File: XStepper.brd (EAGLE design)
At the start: 102 x 82 mm, 95 parts, among them IC1 L7805, IC2 L7812, Q2 16 MHZ, U1 FT232RL-BASICSSOP

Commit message: - some changes from matt and produce in fab 0.95
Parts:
- removed C14, C15: 18pF, resistor:C025-025X050
- removed C16: 0.1uF, resistor:C025-025X050
- removed C17, C19: 0.1uF, SparkFun-Capacitors:1206
- removed C9: 100uF, resistor:E2,5-6
- removed R11: 220, SparkFun-Resistors:AXIAL-0.3
- removed R13, R14: 10K, SparkFun-Resistors:1206
- removed R3, R6, R7: 330, SparkFun-Resistors:AXIAL-0.3
- removed R5: 110, SparkFun-Resistors:AXIAL-0.3
- removed R8, R9: 1K, SparkFun-Resistors:1206
- added C22, C30, C31: 0.1uF, resistor:C025-025X050
- added C32: 10uF, SparkFun-Capacitors:EIA3216
- added C33, C34: 0.1uF, SparkFun-Capacitors:1206
- added JP9: (no value), SparkFun-Connectors:1X02
- added R21, R32, R33: 330, SparkFun-Resistors:AXIAL-0.3
- added R30, R31: 470, SparkFun-Resistors:AXIAL-0.3
- added R34, R35: 10K, SparkFun-Resistors:1206
- added R36, R37: 1K, SparkFun-Resistors:1206
- added SJ1: NO, SparkFun-Passives:SJ_2S-NO
- A-AXIS, X-AXIS, Y-AXIS, Z-AXIS: value 2x03 -> (none)
- AD, XD, YD, ZD: value green -> Gr
- C1: value 0.1uF -> 18pF
- C10: value 47uF -> 200uF; device resistor:E2,5-6 -> resistor:E3,5-8
- C11: value 0.1uF -> 100uF; device resistor:C025-025X050 -> resistor:E2,5-6
- C12: value 0.1uF -> 47uF; device resistor:C025-025X050 -> resistor:E2,5-6
- C2: value 100uF -> 18pF; device resistor:E3,5-8 -> resistor:C025-025X050
- C20: value 10uF -> 0.1uF; device SparkFun-Capacitors:EIA3216 -> resistor:C025-025X050
- C21: value 200uF -> 100uF
- R10, R25: value 220 -> 330
- R22: value 470 -> 110
- R23: value 470 -> 330
- VCC: value orange -> Or
- X, Y, Z: value red -> Rd
- moved C13 85.2 mm to (8.89, 16.5)
- moved C2 64.9 mm to (54.6, 19.1), turned to 270 degrees
- moved C20 63.3 mm to (26.2, 64.2), turned to 0 degrees
- moved R22 55.8 mm to (44.7, 45.9), turned to 0 degrees
- moved C1 52.1 mm to (52.1, 19.1), turned to 270 degrees
- moved C3 40.8 mm to (45.0, 23.5), turned to 90 degrees
- moved R10 35.1 mm to (20.3, 11.4), turned to 0 degrees
- moved C21 33.2 mm to (12.0, 68.0), turned to 270 degrees
- moved R23 26.7 mm to (62.4, 4.83), turned to 90 degrees
- moved C12 26.2 mm to (20.3, 17.8)
- moved JP6 23.9 mm to (87.1, 12.4)
- moved C10 16.6 mm to (20.3, 34.3), turned to 270 degrees
- moved SJ4 16.3 mm to (90.2, 12.3)
- moved C11 14.5 mm to (20.3, 25.4)
- moved TX 8.13 mm to (89.6, 42.9)
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- renumbered C4 to C23, C5 to C24, C6 to C25, C7 to C26, C8 to C27, R12 to R25, R15 to R24, R16 to R26, R4 to R20
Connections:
- new net N$10: SJ1.1, TTL.2
- new net USB_GND: C32.C, C33.2, C34.2, JP7.GND, JP8.GND, JP9.1, SJ1.2, SJ4.2, TTL.1, U1.18, U1.21, U1.25, U1.26, U1.7
- net +12V: now also C11.+; no longer C9.+
- net 5V: now also C12.+, C13.2, C20.1, C22.1, C3.2, C31.2, R10.P$2, R32.P$2, R36.2, R37.2; no longer C1.1, C10.+, C11.2, C12.2, C16.2, C3.1, R3.P$2, R6.P$2, R8.2, R9.2
- net DTR: now also C30.1, R35.2; no longer C13.1, R13.2
- net FTDI_TX: now also R34.2; no longer R14.2
- net GND: now also C11.-, C12.-, C13.1, C2.2, C20.2, C22.2, C3.1, C31.1, JP9.2, R22.P$2; no longer C11.1, C12.1, C14.2, C15.2, C16.1, C17.2, C19.2, C2.-, C20.C, C3.2, C9.-, JP7.GND, JP8.GND, R5.P$2, SJ4.2, TTL.1, U1.18, U1.21, U1.25, U1.26, U1.7
- net N$1: now also C34.1; no longer C17.1
- net N$17: now also R37.1; no longer R9.1
- net N$18: now also R36.1; no longer R8.1
- net N$25: now also R22.P$1; no longer R5.P$1
- net N$33: now also C1.1; no longer C15.1
- net N$34: now also C2.1; no longer C14.1
- net N$35: now also R21.P$2; no longer R10.P$2
- net N$36: now also R23.P$2; no longer R11.P$2
- net N$4: now also R35.1; no longer R13.1
- net N$43: now also R10.P$1; no longer R3.P$1
- net N$46: now also R31.P$2; no longer R23.P$2
- net N$47: now also R30.P$2; no longer R22.P$2
- net N$9: now also R34.1; no longer R14.1
- net OPTO_RX: now also R33.P$1; no longer R7.P$1
- net OPTO_TX: now also R30.P$1; no longer R22.P$1
- net RESET: now also C30.2; no longer C13.2
- net RXD_USB: now also R31.P$1; no longer R23.P$1
- net TTL/USB_5V: now also C32.A, C33.1, R33.P$2; no longer C19.1, C20.A, R7.P$2
- net TXD_USB: now also R32.P$1; no longer R6.P$1
- net VIN: now also C10.+; no longer C21.+
- net VMOT: now also C21.+; no longer C2.+
- net X-STOP: now also R21.P$1; no longer R10.P$1
- net Y-STOP: now also R23.P$1; no longer R11.P$1
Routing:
- net RXD_USB: track 56.1 -> 9.85 mm
- net 5V: track 437.5 -> 403.9 mm
- net USB_GND: track 0.00 -> 28.1 mm, vias 0 -> 6
- net SPINDLE-DIR: track 112.7 -> 132.8 mm
- net OPTO_TX: track 31.5 -> 12.0 mm
- net TTL/USB_5V: track 108.7 -> 90.0 mm
- net TTL_RX: track 29.3 -> 11.9 mm
- net TTL_TX: track 28.9 -> 11.9 mm
- net FTDI_RX: track 22.1 -> 6.76 mm, vias 1 -> 0
- net FTDI_TX: track 19.9 -> 5.04 mm
- net SPINDLE-ENABLE: track 130.3 -> 116.5 mm, vias 1 -> 0
- net N$11: track 14.9 -> 26.5 mm
- net ENABLE: track 150.2 -> 138.8 mm
- net GND: track 11.1 -> 0.19 mm, vias 13 -> 1
- net RESET: track 104.3 -> 93.6 mm
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- added copper zone on layer 1, net USB_GND
- added copper zone on layer 16, net USB_GND
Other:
- board text added: "DTR"
- board text added: "RX"
- board text added: "TX"
- board text added: "XStepper 0.95P"
- board text removed: "XStepper 0.95k"

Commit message: - gerber files for ITEAD 0.96
- new pic for docs
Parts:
- removed EN: EN, SparkFun-Passives:SJ_2W
- removed S1: (no value), SparkFun-Electromechanical:TACTILE_SWITCH_SMD
- added S2: (no value), SparkFun-Electromechanical:TACTILE_SWITCH_SMD
- added STEP: EN, SparkFun-Passives:SJ_2W
- JP5, JP6: device SparkFun-Connectors:2X3_POGO -> pinhead:2X03
- JP9: value (none) -> M02PTH
- moved JP5 34.9 mm to (71.1, 34.3), turned to 90 degrees
- moved R33 13.0 mm to (65.5, 13.7), turned to 180 degrees
- moved C31 12.4 mm to (73.0, 26.6), turned to 0 degrees
- moved R31 9.95 mm to (62.0, 20.1), turned to 270 degrees
- moved TX 8.13 mm to (83.2, 37.9)
- moved R32 7.93 mm to (76.5, 29.2), turned to 270 degrees
- moved R2 6.55 mm to (65.7, 33.0)
- moved C1 4.41 mm to (48.3, 21.3), turned to 180 degrees
- moved R20 3.28 mm to (20.5, 46.0)
- moved R22 3.17 mm to (41.5, 46.0)
- moved R24 3.14 mm to (62.5, 46.0)
- moved R26 3.06 mm to (83.5, 46.0)
- moved 328P 2.84 mm to (45.7, 33.0)
- moved RX 2.84 mm to (88.3, 37.9)
- moved JP6 2.83 mm to (84.6, 11.1)
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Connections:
- net 5V: no longer R36.2, R37.2
- net A-STEP: now also STEP.2; no longer EN.2
- net BT_RXD: now also JP5.6; no longer JP5.P$6
- net BT_TXD: now also JP5.5; no longer JP5.P$5
- net FTDI_RX: now also JP6.6; no longer JP6.P$6
- net FTDI_TX: now also JP6.5; no longer JP6.P$5
- net GND: now also S2.1, S2.2; no longer S1.1, S1.2
- net OPTO_RX: now also JP6.4; no longer JP6.P$4
- net OPTO_TX: now also JP6.3; no longer JP6.P$3
- net RESET: now also S2.3, S2.4; no longer S1.3, S1.4
- net RX: now also JP5.3; no longer JP5.P$3
- net RXD_USB: now also JP5.2; no longer JP5.P$2
- net SPINDLE-ENABLE: now also STEP.1; no longer EN.1
- net TTL/USB_5V: now also R36.2, R37.2
- net TTL_RX: now also JP6.2; no longer JP6.P$2
- net TTL_TX: now also JP6.1; no longer JP6.P$1
- net TX: now also JP5.4; no longer JP5.P$4
- net TXD_USB: now also JP5.1; no longer JP5.P$1
- net Y-STEP: now also STEP.3; no longer EN.3
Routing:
- net GND: track 0.19 -> 49.4 mm, vias 1 -> 5
- net BT_TXD: track 72.3 -> 27.3 mm, vias 1 -> 0
- net TX: track 13.3 -> 56.3 mm
- net RX: track 18.4 -> 60.1 mm
- net TXD_USB: track 56.4 -> 17.0 mm
- net 5V: track 403.9 -> 438.6 mm, vias 0 -> 4
- net BT_RXD: track 64.5 -> 30.9 mm
- net TTL/USB_5V: track 90.0 -> 121.9 mm, vias 0 -> 2
- net USB_GND: track 28.1 -> 9.32 mm, vias 6 -> 3
- net SPINDLE-ENABLE: track 116.5 -> 130.5 mm, vias 0 -> 1
- net G-RESET: track 47.5 -> 37.5 mm, vias 0 -> 1
- net RESERVED: track 35.4 -> 44.8 mm
- net N$46: track 13.9 -> 4.90 mm
- net ENABLE: track 138.8 -> 147.8 mm, vias 0 -> 5
- net COOLANT-FLOOD: track 42.5 -> 51.4 mm
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- removed copper zone on layer 1, net GND
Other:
- board size 102 x 82 mm -> 99.7 x 82 mm
- board text added: "+"
- board text added: "-"
- board text added: "XStepper 0.96"
- board text removed: "XStepper 0.95P"

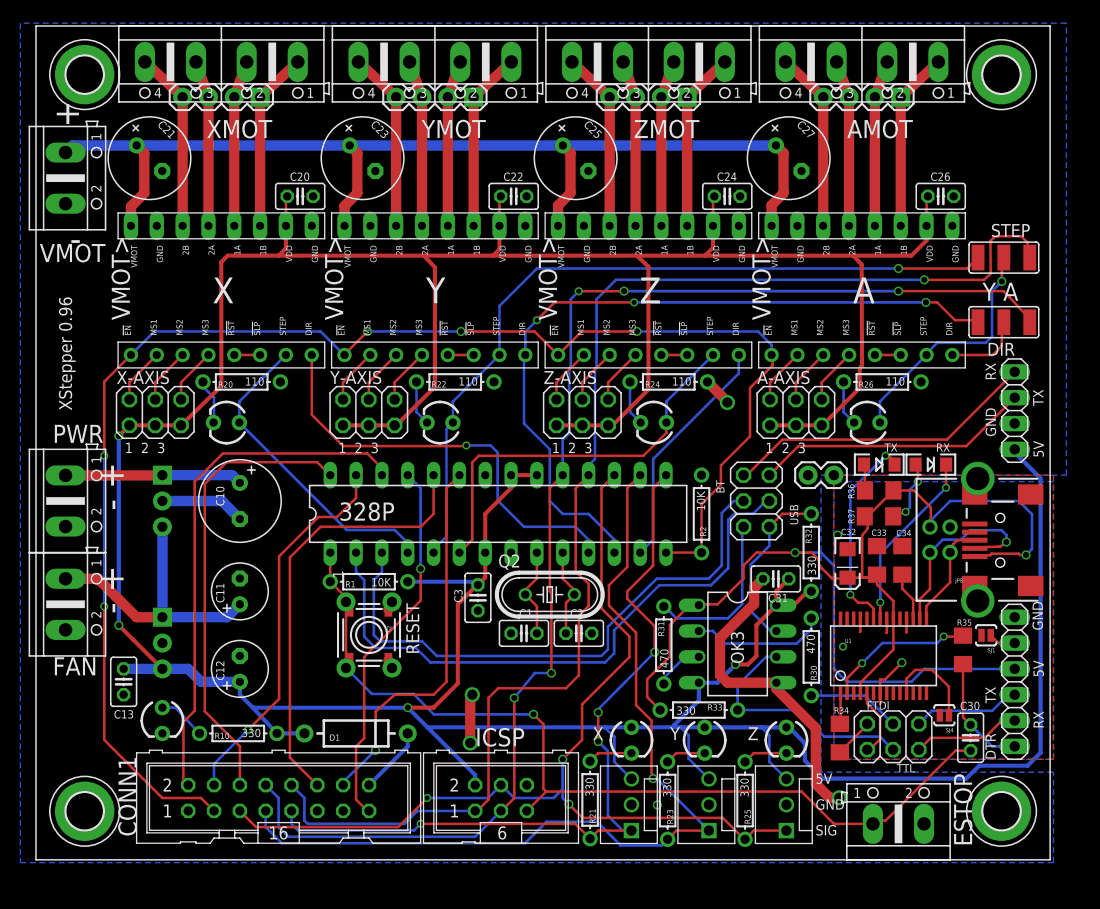
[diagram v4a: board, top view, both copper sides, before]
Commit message: - version 0.97 to fab
*On-board USB in now in the bottom of the board
*USB isolation header moved.
*Bluetooth header moved
*Bluetooth dip/jumpers removed - bluetooth is always-on
*FTDI header moved
*FTDI now can be tied to 5V and GND for isolation or to forego isolation
and directly power the board logic from USB
*Pololu jumpers now separated (I forgot that this was a requirement and
not an option)
*Removed endstop status LED's
*Removed 16-pin header
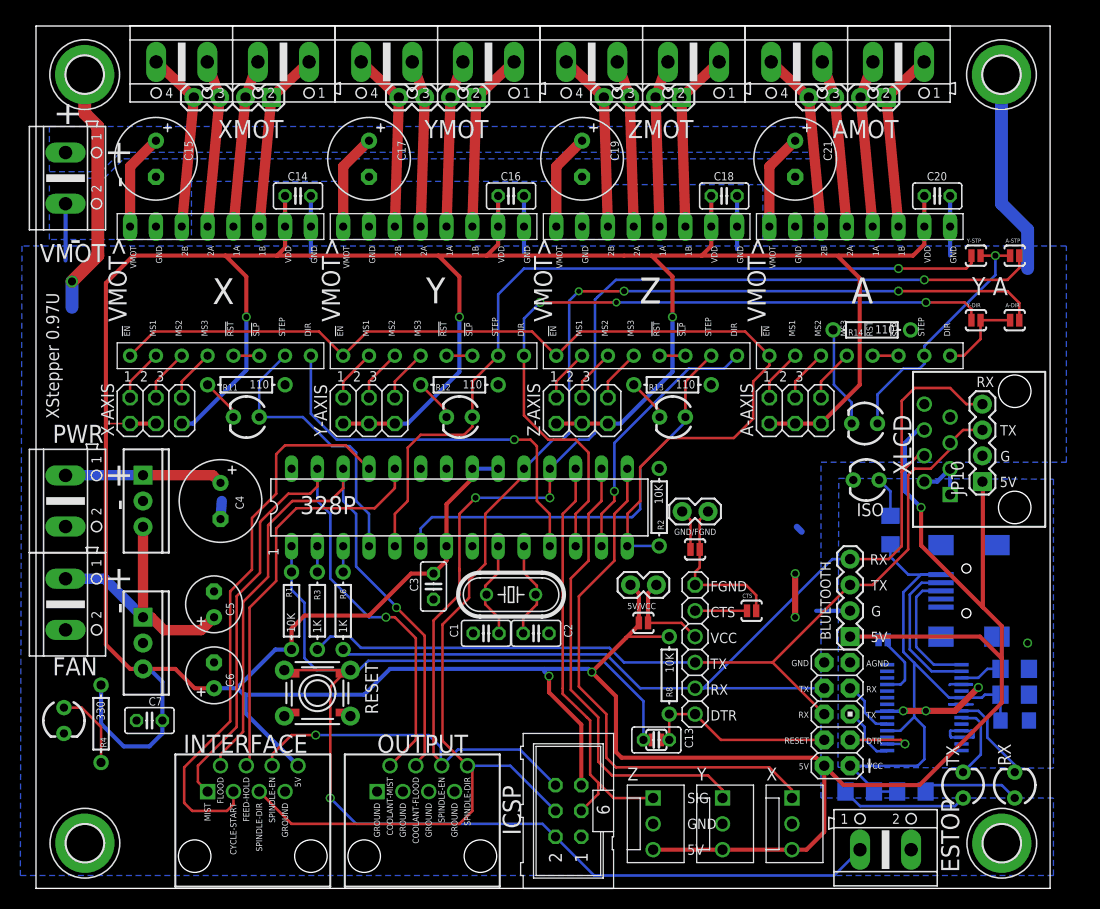
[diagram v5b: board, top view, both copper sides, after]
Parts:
- removed BT-TTL: (no value), pinhead:1X04
- removed C22, C24, C26, C30, C31: 0.1uF, resistor:C025-025X050
- removed C23, C25, C27: 100uF, resistor:E3,5-8
- removed C32: 10uF, SparkFun-Capacitors:EIA3216
- removed C33, C34: 0.1uF, SparkFun-Capacitors:1206
- removed CONN1: (no value), con-ml:ML16
- removed D1: (no value), SparkFun-DiscreteSemi:DIODE-1N4001
- removed DIR: DIR, SparkFun-Passives:SJ_2W
- removed ICSP: (no value), con-ml:ML6
- removed JP8: USB-B, SparkFun-Connectors:USB-B-PTH
- removed OK3: HCPL2630, optocoupler:DIL08
- removed R20, R22, R24, R26: 110, SparkFun-Resistors:AXIAL-0.3
- removed R21, R23, R25, R32, R33: 330, SparkFun-Resistors:AXIAL-0.3
- removed R30, R31: 470, SparkFun-Resistors:AXIAL-0.3
- removed R34, R35: 10K, SparkFun-Resistors:1206
- removed R36, R37: 1K, SparkFun-Resistors:1206
- removed SJ1, SJ4: NO, SparkFun-Passives:SJ_2S-NO
- removed STEP: EN, SparkFun-Passives:SJ_2W
- removed TTL: GND, pinhead:1X06
- removed X, Y, Z: Rd, SparkFun-LED:LED3MM
- added 5V, A-DIR, A-STP, CTS, CTS-FTDI, DTR, GND, Y-DIR, Y-STP: NO, SparkFun-Passives:SJ_2S-NO
- added C14, C16, C18, C7: 0.1uF, resistor:C025-025X050
- added C15, C17, C19: 100uF, resistor:E3,5-8
- added C4: 200uF, resistor:E3,5-8
- added C5: 100uF, resistor:E2,5-6
- added C6: 47uF, resistor:E2,5-6
- added ISO: (no value), SparkFun-LED:LED3MM
- added JP10, JP11: (no value), SparkFun-Connectors:1X04
- added JP12: (no value), pinhead:1X06
- added R11, R12, R13, R14: 110, SparkFun-Resistors:AXIAL-0.3
- added R3, R6: 1K, SparkFun-Resistors:AXIAL-0.3
- added R4: 330, SparkFun-Resistors:AXIAL-0.3
- added R5, R9: 1K, SparkFun-Resistors:1206
- added R8: 10K, SparkFun-Resistors:AXIAL-0.3
- added SV1: (no value), con-ml:ML6
- added U$14, U$2, U$8: TYCO 5555164-1, SparkFun-Connectors:RJ45-8
- C10: value 200uF -> 10uF; device resistor:E3,5-8 -> SparkFun-Capacitors:EIA3216
- C11: value 100uF -> 0.1uF; device resistor:E2,5-6 -> SparkFun-Capacitors:1206
- C12: value 47uF -> 0.1uF; device resistor:E2,5-6 -> SparkFun-Capacitors:1206
- JP5: value (none) -> M05X2PTH; device pinhead:2X03 -> SparkFun-Connectors:AVR_ICSP
- JP6: value (none) -> M02PTH; device pinhead:2X03 -> SparkFun-Connectors:1X02
- R10: value 330 -> 1K; device SparkFun-Resistors:AXIAL-0.3 -> SparkFun-Resistors:1206
- RX: value Grn -> (none); device SparkFun-LED:LED-1206 -> SparkFun-LED:LED3MM
- TX: value Red -> (none); device SparkFun-LED:LED-1206 -> SparkFun-LED:LED3MM
- moved C10 79.2 mm to (96.5, 12.7), flipped to the bottom, turned to 0 degrees
- moved C11 76.9 mm to (96.5, 15.2), flipped to the bottom, turned to 180 degrees
- moved C12 76.2 mm to (96.5, 17.8), flipped to the bottom, turned to 180 degrees
- moved C21 63.5 mm to (74.9, 67.9), turned to 270 degrees
- moved C20 62.7 mm to (88.9, 64.3)
- moved R10 61.4 mm to (81.3, 5.71), flipped to the bottom, turned to 180 degrees
- moved C13 52.7 mm to (61.3, 10.8), turned to 180 degrees
- moved RX 32.6 mm to (96.5, 6.35), turned to 90 degrees
- moved TX 32.6 mm to (91.4, 6.35), turned to 90 degrees
- moved JP6 27.7 mm to (61.3, 26.0)
- moved JP5 22.4 mm to (79.1, 13.3), turned to 180 degrees
- moved XLIM 16.1 mm to (74.6, 5.08), turned to 270 degrees
- moved JP9 15.3 mm to (63.8, 33.3), turned to 0 degrees
- moved ZLIM 13.5 mm to (61.0, 5.08), turned to 270 degrees
- moved VCC 9.68 mm to (3.02, 12.7)
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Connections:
- removed net BT_RXD: BT-TTL.4, JP5.6
- removed net BT_TXD: BT-TTL.3, JP5.5
- removed net N$35: R21.P$2, X.K
- removed net N$36: R23.P$2, Y.K
- removed net N$37: R25.P$2, Z.K
- removed net N$45: CONN1.16, D1.C
- removed net N$46: OK3.3, R31.P$2
- removed net N$47: OK3.2, R30.P$2
- removed net OPTO_RX: JP6.4, OK3.6, R33.P$1
- removed net OPTO_TX: JP6.3, R30.P$1
- removed net RXD_USB: JP5.2, R31.P$1
- removed net TTL/USB_5V: C32.A, C33.1, JP7.VBUS, JP8.VBUS, OK3.1, R33.P$2, R36.2, R37.2, TTL.3, U1.20, U1.4
- removed net TTL_RX: JP6.2, TTL.5
- removed net TTL_TX: JP6.1, TTL.4
- removed net TXD_USB: JP5.1, OK3.7, R32.P$1
- removed net USB_GND: C32.C, C33.2, C34.2, JP7.GND, JP8.GND, JP9.1, SJ1.2, SJ4.2, TTL.1, U1.18, U1.21, U1.25, U1.26, U1.7
- removed net VMOT: C21.+, C23.+, C25.+, C27.+, STEPPERDRIVER.VMOT, STEPPERDRIVER1.VMOT, STEPPERDRIVER2.VMOT, STEPPERDRIVER3.VMOT, VMOT.1
- new net AGND: C10.C, C11.2, C12.2, CTS-FTDI.2, ISO.K, JP5.9, JP7.GND, U1.18, U1.21, U1.25, U1.26, U1.7
- new net FTDI_DTR: JP5.3, U1.2
- new net N$40: 328P.3, R6.P$1
- new net N$41: 5V.1, JP12.3, JP6.1
- new net N$44: CTS.2, GND.1, JP12.1, JP9.2
- new net V+: C15.+, C17.+, C19.+, C21.+, STEPPERDRIVER.VMOT, STEPPERDRIVER1.VMOT, STEPPERDRIVER2.VMOT, STEPPERDRIVER3.VMOT, VMOT.1
- new net VCC/2: C10.A, C11.1, JP5.1, JP7.VBUS, R10.2, R5.2, R9.2, U1.20, U1.4
- net +12V: now also C5.+; no longer C11.+
- net 5V: now also 5V.2, C14.1, C16.1, C18.1, C6.+, C7.2, JP10.1, JP11.1, JP5.2, JP6.2, R4.P$2, R8.P$2, SV1.5, U$14.6, U$2.8; no longer BT-TTL.1, C12.+, C13.2, C22.1, C24.1, C26.1, C31.2, D1.A, ICSP.2, OK3.4, OK3.8, R10.P$2, R32.P$2, X.A, Y.A, Z.A
- net A-DIR: now also A-DIR.1, Y-DIR.2; no longer DIR.2
- net A-STEP: now also A-STP.1, Y-STP.2; no longer STEP.2
- net COOLANT-FLOOD: now also U$2.2, U$8.4; no longer CONN1.2
- net COOLANT-MIST: now also U$2.1, U$8.2; no longer CONN1.4
- net CYCLE-START: now also U$2.3; no longer CONN1.15
- net DTR: now also C13.1, DTR.1, JP12.6, JP5.4, R8.P$1; no longer C30.1, R35.2, TTL.6
- net ENABLE: no longer CONN1.3
- net FEED-HOLD: now also U$2.4; no longer CONN1.12
- net FTDI_RX: now also JP5.7; no longer JP6.6
- net FTDI_TX: now also JP5.5, U1.1; no longer JP6.5, R34.2
- net G-RESET: no longer CONN1.14
- net GND: now also C14.2, C15.-, C16.2, C17.-, C18.2, C19.-, C4.-, C5.-, C6.-, C7.1, GND.2, JP10.2, JP11.2, JP5.10, JP9.1, R11.P$2, R12.P$2, R13.P$2, R14.P$2, SV1.1, U$14.1, U$14.2, U$14.3, U$14.7, U$14.8, U$2.7, U$8.1, U$8.3, U$8.5, U$8.7; no longer BT-TTL.2, C10.-, C11.-, C12.-, C13.1, C22.2, C23.-, C24.2, C25.-, C26.2, C27.-, C31.1, CONN1.1, CONN1.11, CONN1.13, ICSP.6, JP9.2, OK3.5, R20.P$2, R22.P$2, R24.P$2, R26.P$2
- net N$1: now also C12.1; no longer C34.1
- net N$10: now also CTS.1, JP12.2; no longer SJ1.1, TTL.2
- net N$11: now also TX.K; no longer TX.C
- net N$12: now also RX.K; no longer RX.C
- net N$17: now also R9.1; no longer R37.1
- net N$18: now also R10.1; no longer R36.1
- net N$19: now also CTS-FTDI.1; no longer SJ4.1
- net N$2: no longer JP8.D+
- net N$20: now also R11.P$1; no longer R20.P$1
- net N$25: now also R12.P$1; no longer R22.P$1
- net N$26: now also R13.P$1; no longer R24.P$1
- net N$28: now also R14.P$1; no longer R26.P$1
- net N$3: no longer JP8.D-
- net N$4: now also ISO.A, R5.1; no longer R35.1, U1.2
- net N$43: now also R4.P$1; no longer R10.P$1
- net N$9: now also 328P.2, R3.P$1; no longer R34.1, U1.1
- net RESERVED: no longer CONN1.6
- net RESET: now also C13.2, DTR.2, SV1.2; no longer C30.2, ICSP.5
- net RX: now also JP10.3, JP11.3, JP12.4, JP5.6, R3.P$2, U$14.5; no longer 328P.2, JP5.3
- net SPINDLE-DIR: now also A-DIR.2, SV1.4, U$2.5, U$8.8; no longer CONN1.8, DIR.3, ICSP.3
- net SPINDLE-ENABLE: now also A-STP.2, SV1.6, U$2.6, U$8.6; no longer CONN1.10, ICSP.1, STEP.1
- net TX: now also JP10.4, JP11.4, JP12.5, JP5.8, R6.P$2, U$14.4; no longer 328P.3, JP5.4
- net VIN: now also C4.+; no longer C10.+
- net X-STOP: no longer CONN1.9, R21.P$1
- net Y-DIR: now also Y-DIR.1; no longer DIR.1
- net Y-STEP: now also Y-STP.1; no longer STEP.3
- net Y-STOP: no longer CONN1.7, R23.P$1
- net Z-STOP: now also SV1.3; no longer CONN1.5, ICSP.4, R25.P$1
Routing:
- net TTL/USB_5V: track 121.9 -> 0.00 mm, vias 2 -> 0
- net VMOT: track 105.1 -> 0.00 mm
- net 5V: track 438.6 -> 525.4 mm, vias 4 -> 6
- net VCC/2: track 0.00 -> 57.8 mm
- net Z-STOP: track 95.2 -> 42.4 mm, vias 3 -> 0
- net ENABLE: track 147.8 -> 100.2 mm, vias 5 -> 0
- net GND: track 49.4 -> 94.7 mm, vias 5 -> 3
- net RESERVED: track 44.8 -> 0.00 mm
- net TX: track 56.3 -> 100.5 mm
- net Y-STOP: track 88.8 -> 45.3 mm, vias 1 -> 0
- net V+: track 0.00 -> 38.0 mm
- net RESET: track 91.6 -> 129.3 mm
- net G-RESET: track 37.5 -> 0.00 mm, vias 1 -> 0
- net COOLANT-MIST: track 37.3 -> 74.0 mm
- net BT_RXD: track 30.9 -> 0.00 mm
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- added copper zone on layer 16, net AGND
- added copper zone on layer 16, net V+
- removed copper zone on layer 1, net USB_GND
- removed copper zone on layer 16, net USB_GND
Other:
- board size 99.7 x 82 mm -> 99.7 x 84.8 mm
- board text added: "5V/VCC"
- board text added: "AGND"
- board text added: "BLUETOOTH"
- board text added: "COOLANT-FLOOD"
- board text added: "COOLANT-MIST"
- board text added: "CTS"
- board text added: "CYCLE-START"
- board text added: "FEED-HOLD"
- board text added: "FGND"
- board text added: "FLOOD"
- board text added: "G"
- board text added: "GND/FGND"
- board text added: "GROUND"
- board text added: "ICSP"
- board text added: "INTERFACE"
- board text added: "MIST"
- board text added: "OUTPUT"
- board text added: "RESET"
- board text added: "SPINDLE-DIR"
- board text added: "SPINDLE-EN"
- board text added: "VCC"
- board text added: "XLCD"
- board text added: "XStepper 0.97U"
- board text removed: "BT"
- board text removed: "FTDI"
- board text removed: "TTL"
- board text removed: "USB"
- board text removed: "XStepper 0.96"
